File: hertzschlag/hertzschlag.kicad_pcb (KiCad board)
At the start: 2 copper layers, 85.5 x 28 mm, 29 parts, among them IC1 TB67H450FNG,EL, IC2 TB67H450FNG,EL, J1 TB_1X2, J12 Conn_01x04_Female, J14 Conn_01x03_Male, J17 Conn_01x30_Pin, J2 Conn_01x03_Male, J4 MotorA, J5 MotorB, SW1 SW_Push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

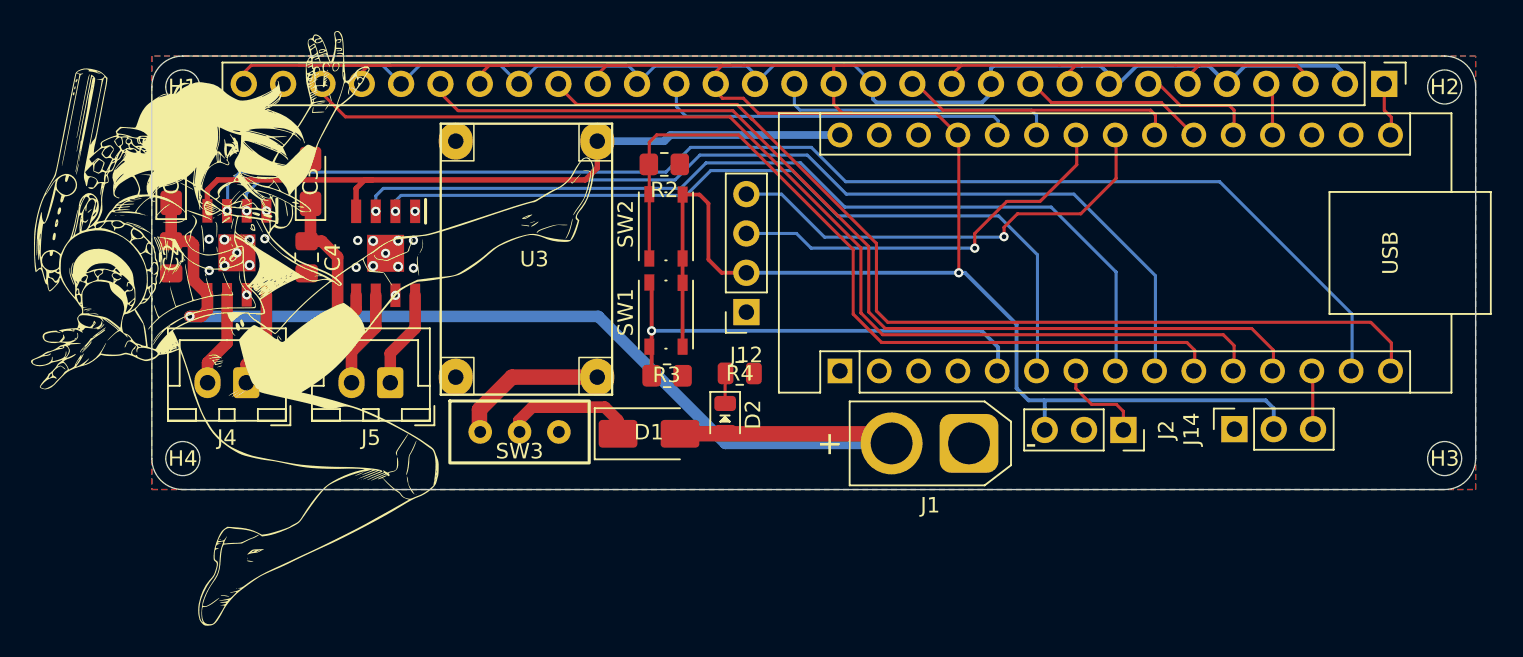
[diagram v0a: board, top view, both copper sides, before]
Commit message: Changes on PCB.
Changes to Footprints, Routing, Alignment.
And no more falling alita on the front Silk screen (sad).
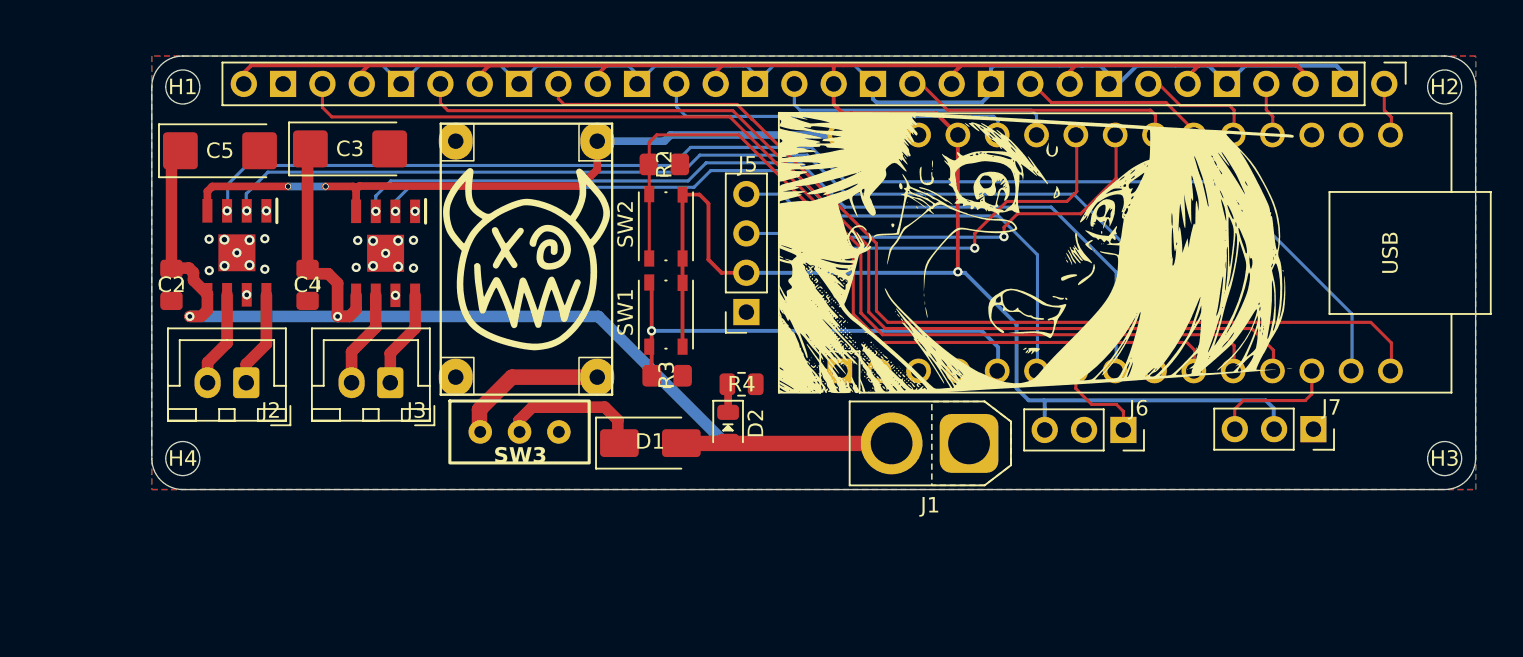
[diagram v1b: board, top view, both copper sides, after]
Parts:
- removed the G*** at (119.0, 100.5)
- added G***: LOGO, AJ_IMG:Alita Angry, F.Cu at (166.1, 95.7)
- added G***: LOGO, AJ_IMG:JVB, F.Cu at (133.2, 96.1)
- C3, C5: footprint Capacitor_Tantalum_SMD:CP_EIA-3216-18_Kemet-A_HandSolder -> Capacitor_Tantalum_SMD:CP_EIA-6032-15_Kemet-U_HandSolder
- moved J7 5.11 mm to (184.0, 107.1), turned to -90 degrees
- moved C5 3.69 mm to (113.4, 89.1), turned to 0 degrees
- moved C3 3.30 mm to (121.8, 89.0), turned to 0 degrees
- moved C4 1.78 mm to (119.1, 97.8)
- moved C2 1.78 mm to (110.3, 97.8)
- moved R4 0.71 mm to (147.1, 104.2)
- moved D1 0.61 mm to (141.2, 108.0)
- moved D2 0.60 mm to (146.2, 106.8)
- renumbered J4 to J2, J5 to J3, J17 to J4, J12 to J5, J2 to J6, J14 to J7
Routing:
- net +5V: track 176.1 -> 166.8 mm
- net /VM: track 81.4 -> 88.8 mm
- net /Servo: track 3.76 -> 8.16 mm
- net VCC: track 48.3 -> 47.1 mm, vias 0 -> 2
- net /SCL: track 26.4 -> 27.4 mm
- net /SENSOR0: track 70.8 -> 71.3 mm
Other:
- copper layers 2 -> 4

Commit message: Updated PCB design
Changes to XT30 Connector and routing.
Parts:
- added G***: LOGO, AJ_IMG:HERTZ, F.Cu at (120.9, 109.2)
- added J8: Extra, Connector_PinSocket_2.54mm:PinSocket_1x02_P2.54mm_Vertical, F.Cu at (168.2, 109.2)
- moved J6 7.72 mm to (179.5, 107.2)
- moved J7 4.58 mm to (188.6, 107.2)
- moved J1 1.33 mm to (163.1, 108.0)
- moved R4 1.18 mm to (146.2, 103.4), turned to 90 degrees
- moved J3 0.15 mm to (124.4, 104.0)
- moved J2 0.15 mm to (115.1, 104.0)
- moved D2 0.08 mm to (146.2, 106.7)
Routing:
- net /VM: track 88.8 -> 106.1 mm
- net /MSJS: track 6.09 -> 14.1 mm
- net +5V: track 166.8 -> 171.3 mm
- net /Servo: track 8.16 -> 4.00 mm
